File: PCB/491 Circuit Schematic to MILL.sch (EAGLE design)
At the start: 22 parts, among them J1 DCJ0202, X2 1751248

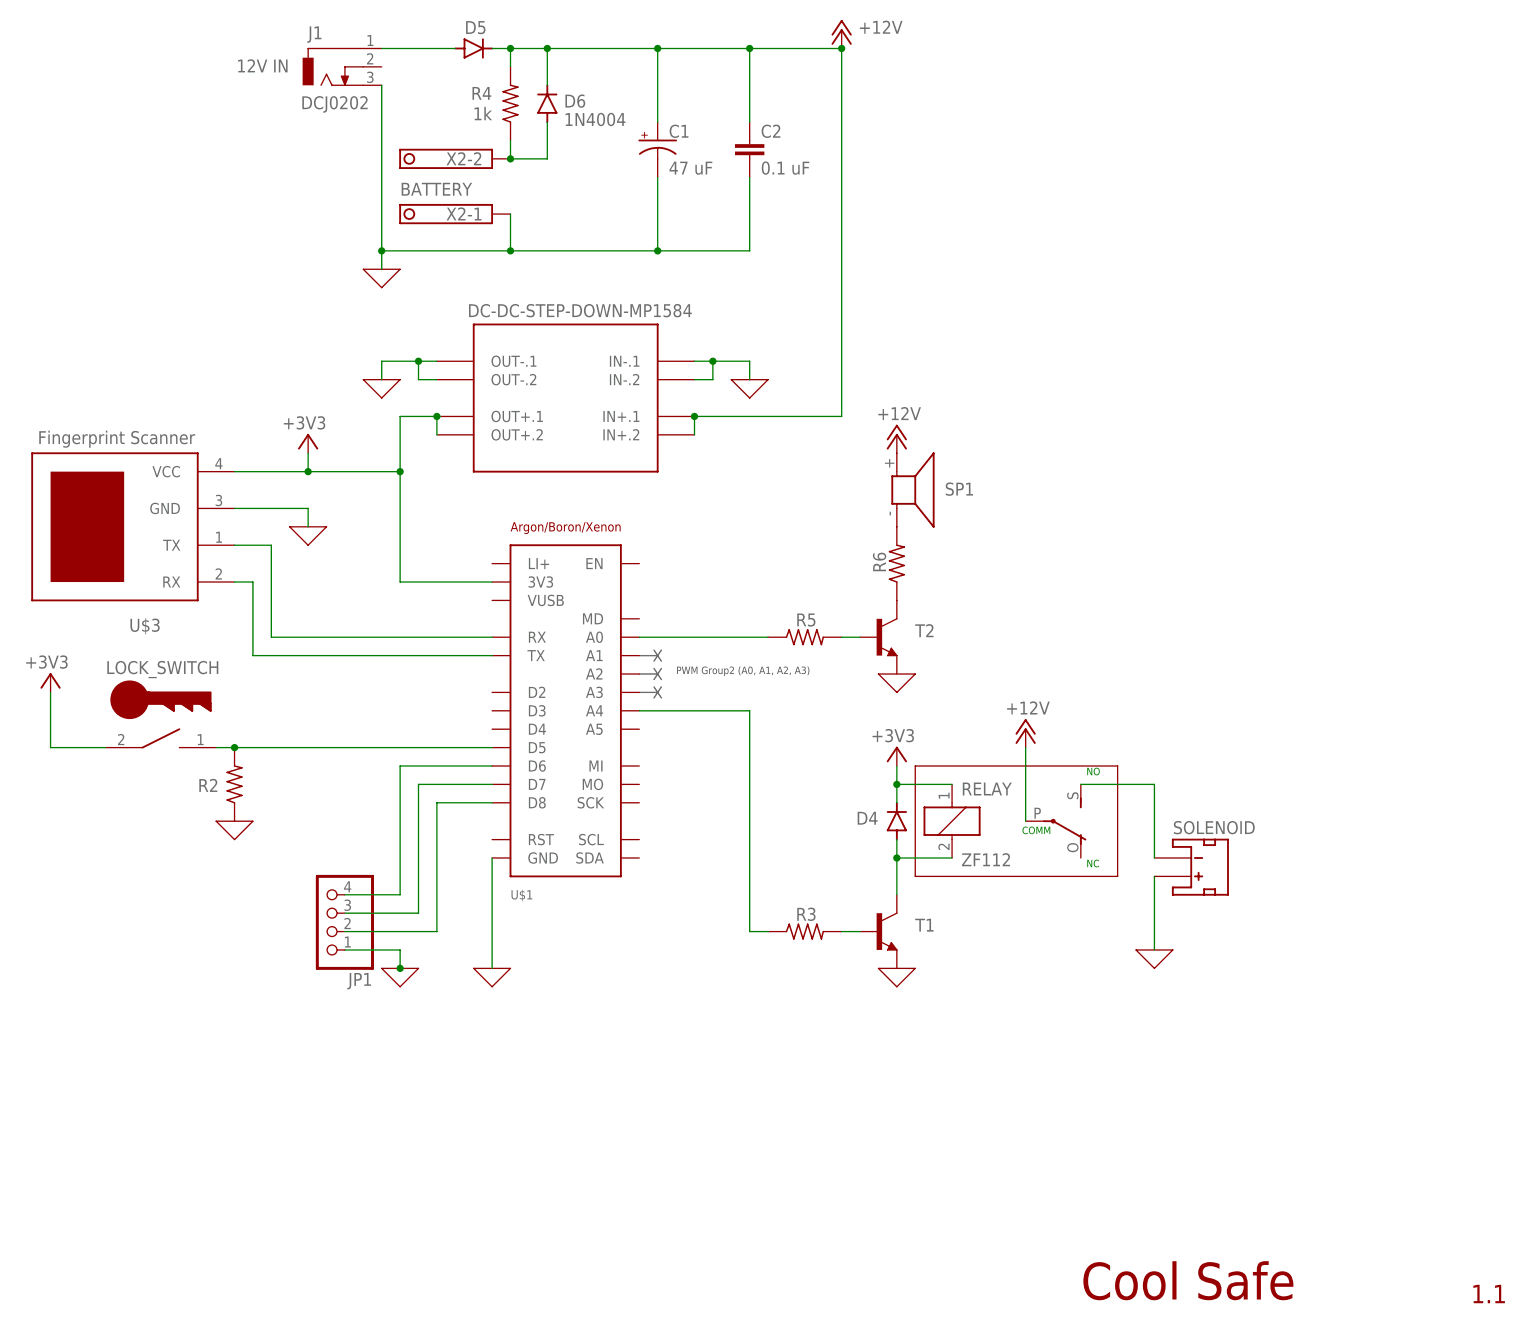
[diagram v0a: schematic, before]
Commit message: PCB V1
Pretty much ready to mill.  Added a to MILL board and some breakout boards for SMT components so that we only need a single-sided copper clad board.
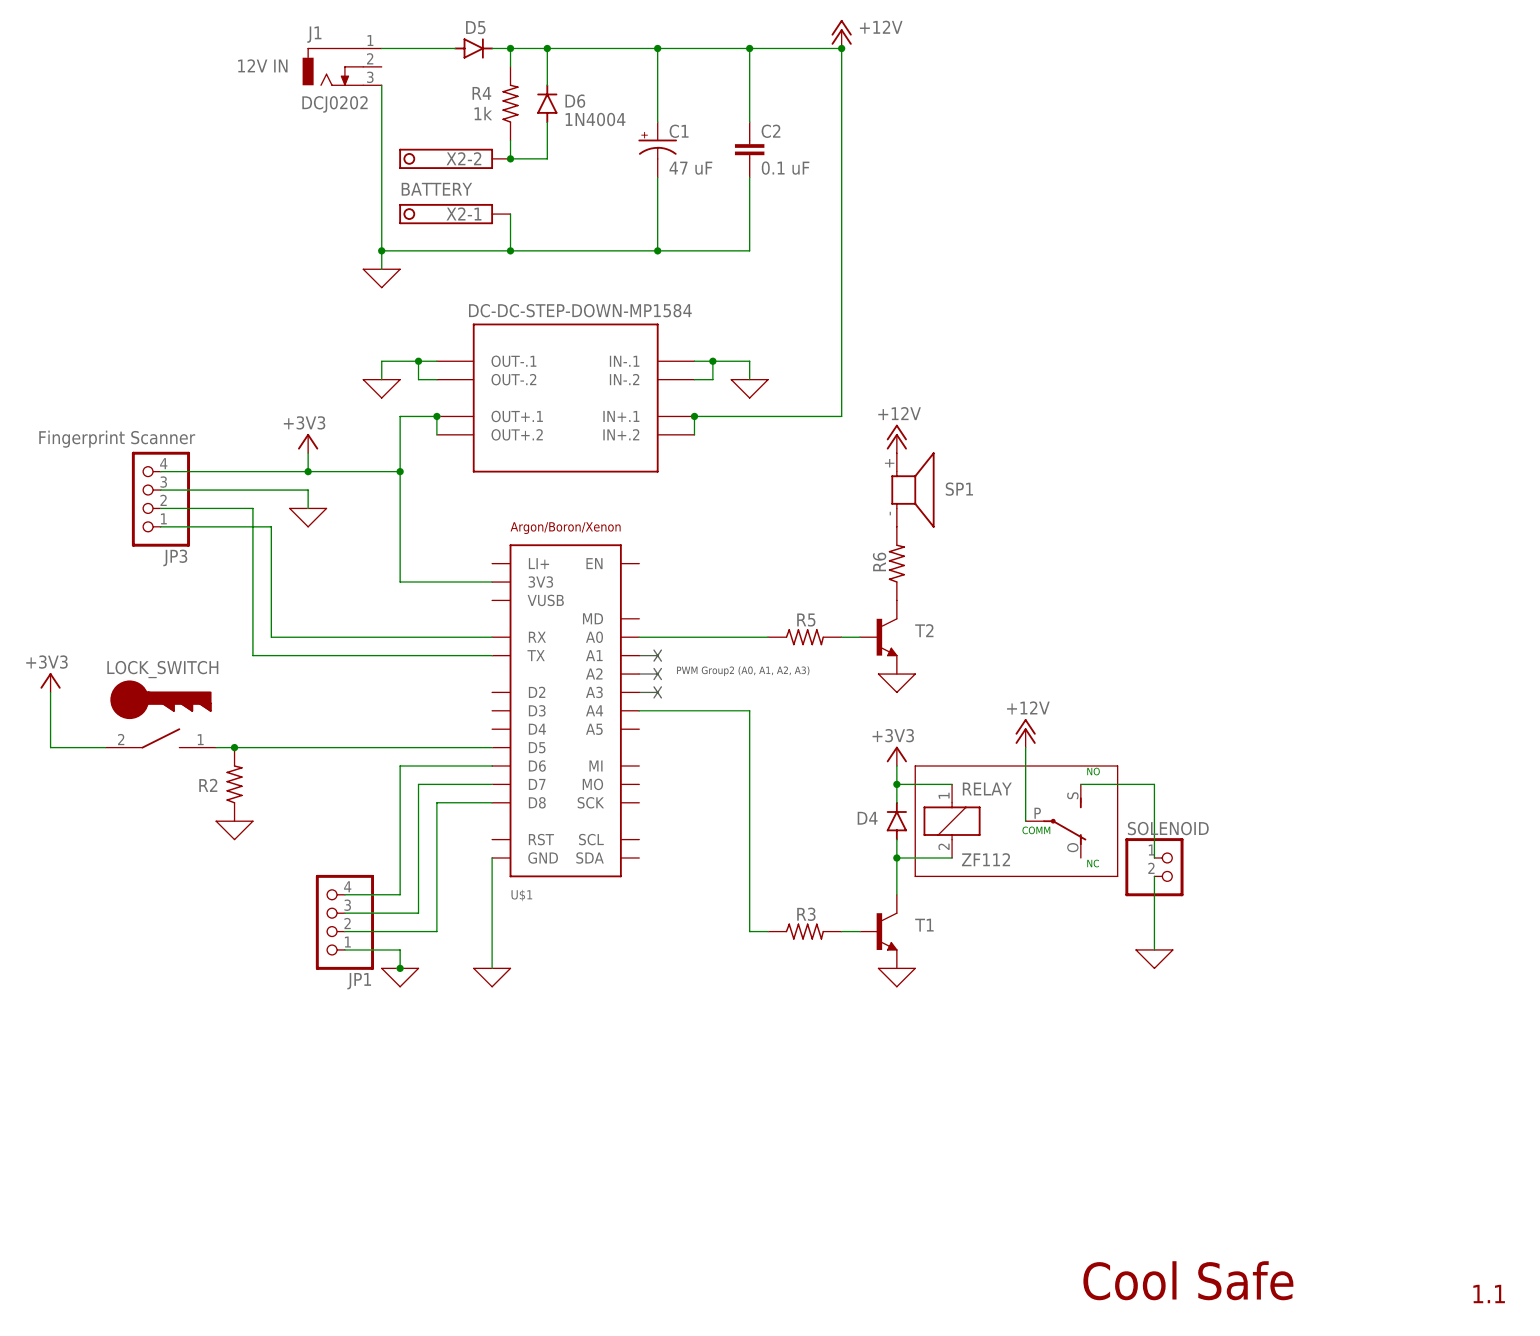
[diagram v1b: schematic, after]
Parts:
- removed U$3: FPSQWIIC, cool_safe_lib:FPSQWIIC
- added JP3: (no value), pinhead:PINHD-1X4
- SOLENOID: device cool_safe_lib:JST_2MM_MALE -> pinhead:PINHD-1X2
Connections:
- net +3V3: now also JP3.4; no longer U$3.VCC
- net 0: now also JP3.3, SOLENOID.2; no longer SOLENOID.+, U$3.GND
- net N$13: now also SOLENOID.1; no longer SOLENOID.-
- net N$16: now also JP3.1; no longer U$3.TX
- net N$28: now also JP3.2; no longer U$3.RX
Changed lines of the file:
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@@
 <part name="RELAY" library="relay" library_urn="urn:adsk.eagle:library:339" deviceset="ZF112" device="" package3d_urn="urn:adsk.eagle:package:24315/1"/>
 <part name="J1" library="con-jack" library_urn="urn:adsk.eagle:library:154" deviceset="DCJ0202" device="" package3d_urn="urn:adsk.eagle:package:7491/1"/>
-<part name="SOLENOID" library="cool_safe_lib" deviceset="JST_2MM_MALE" device="" package3d_urn="urn:adsk.eagle:package:38042/1"/>
-<part name="U$3" library="cool_safe_lib" deviceset="FPS" device="QWIIC"/>
+<part name="SOLENOID" library="pinhead" library_urn="urn:adsk.eagle:library:325" deviceset="PINHD-1X2" device="" package3d_urn="urn:adsk.eagle:package:22435/2"/>
+<part name="JP3" library="pinhead" library_urn="urn:adsk.eagle:library:325" deviceset="PINHD-1X4" device="" package3d_urn="urn:adsk.eagle:package:22407/2"/>
 </parts>
 <sheets>
@@
 <attribute name="VALUE" x="106.68" y="129.54" size="1.778" layer="96" rot="R180"/>
 </instance>
-<instance part="X_11" gate="G$1" x="104.14" y="114.3" smashed="yes"/>
+<instance part="X_11" gate="G$1" x="104.14" y="116.84" smashed="yes"/>
 <instance part="FRAME1" gate="G$1" x="0" y="0" smashed="yes"/>
 <instance part="FRAME1" gate="G$2" x="172.72" y="0" smashed="yes">
@@
 <attribute name="VALUE" x="103.124" y="171.958" size="1.778" layer="96"/>
 </instance>
-<instance part="SOLENOID" gate="G$1" x="226.06" y="68.58" smashed="yes" rot="R270">
-<attribute name="NAME" x="223.52" y="71.882" size="1.778" layer="95"/>
-</instance>
-<instance part="U$3" gate="G$1" x="66.04" y="116.84" smashed="yes" rot="R180">
-<attribute name="NAME" x="83.82" y="101.6" size="1.778" layer="95" rot="R180"/>
+<instance part="SOLENOID" gate="G$1" x="223.52" y="66.04" smashed="yes">
+<attribute name="NAME" x="217.17" y="71.755" size="1.778" layer="95"/>
+<attribute name="VALUE" x="217.17" y="60.96" size="1.778" layer="96"/>
+</instance>
+<instance part="JP3" gate="A" x="81.28" y="119.38" smashed="yes" rot="R180">
+<attribute name="NAME" x="87.63" y="111.125" size="1.778" layer="95" rot="R180"/>
+<attribute name="VALUE" x="87.63" y="127" size="1.778" layer="96" rot="R180"/>
 </instance>
 </instances>
@@
 <pinref part="X_7" gate="G$1" pin="0"/>
 <wire x1="220.98" y1="66.04" x2="220.98" y2="55.88" width="0.1524" layer="91"/>
-<pinref part="SOLENOID" gate="G$1" pin="+"/>
+<pinref part="SOLENOID" gate="G$1" pin="2"/>
 </segment>
 <segment>
@@
 <segment>
 <pinref part="X_11" gate="G$1" pin="0"/>
-<wire x1="104.14" y1="114.3" x2="104.14" y2="116.84" width="0.1524" layer="91"/>
-<wire x1="104.14" y1="116.84" x2="93.98" y2="116.84" width="0.1524" layer="91"/>
-<pinref part="U$3" gate="G$1" pin="GND"/>
+<wire x1="104.14" y1="116.84" x2="104.14" y2="119.38" width="0.1524" layer="91"/>
+<pinref part="JP3" gate="A" pin="3"/>
+<wire x1="104.14" y1="119.38" x2="83.82" y2="119.38" width="0.1524" layer="91"/>
 </segment>
 <segment>
@@
 <wire x1="121.92" y1="127" x2="121.92" y2="129.54" width="0.1524" layer="91"/>
 <junction x="121.92" y="129.54"/>
-<wire x1="104.14" y1="121.92" x2="93.98" y2="121.92" width="0.1524" layer="91"/>
-<pinref part="U$3" gate="G$1" pin="VCC"/>
+<pinref part="JP3" gate="A" pin="4"/>
+<wire x1="104.14" y1="121.92" x2="83.82" y2="121.92" width="0.1524" layer="91"/>
 </segment>
 <segment>
@@
 <pinref part="U$1" gate="G$1" pin="RX"/>
 <wire x1="129.54" y1="99.06" x2="99.06" y2="99.06" width="0.1524" layer="91"/>
-<wire x1="99.06" y1="111.76" x2="99.06" y2="99.06" width="0.1524" layer="91"/>
-<pinref part="U$3" gate="G$1" pin="TX"/>
-<wire x1="99.06" y1="111.76" x2="93.98" y2="111.76" width="0.1524" layer="91"/>
+<pinref part="JP3" gate="A" pin="1"/>
+<wire x1="83.82" y1="114.3" x2="99.06" y2="114.3" width="0.1524" layer="91"/>
+<wire x1="99.06" y1="114.3" x2="99.06" y2="99.06" width="0.1524" layer="91"/>
 </segment>
 </net>
@@
 <pinref part="U$1" gate="G$1" pin="TX"/>
 <wire x1="129.54" y1="96.52" x2="96.52" y2="96.52" width="0.1524" layer="91"/>
-<wire x1="96.52" y1="96.52" x2="96.52" y2="106.68" width="0.1524" layer="91"/>
-<pinref part="U$3" gate="G$1" pin="RX"/>
-<wire x1="96.52" y1="106.68" x2="93.98" y2="106.68" width="0.1524" layer="91"/>
+<wire x1="96.52" y1="96.52" x2="96.52" y2="116.84" width="0.1524" layer="91"/>
+<pinref part="JP3" gate="A" pin="2"/>
+<wire x1="96.52" y1="116.84" x2="83.82" y2="116.84" width="0.1524" layer="91"/>
 </segment>
 </net>
@@
 <wire x1="220.98" y1="78.74" x2="220.98" y2="68.58" width="0.1524" layer="91"/>
 <pinref part="RELAY" gate="2" pin="S"/>
-<pinref part="SOLENOID" gate="G$1" pin="-"/>
-</segment>
-</net>
+<pinref part="SOLENOID" gate="G$1" pin="1"/>
+</segment>
+</net>
